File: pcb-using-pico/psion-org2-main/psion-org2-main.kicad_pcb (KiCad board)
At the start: 2 copper layers, 70 x 106 mm, 92 parts, among them J1 Conn_01x24_Female, J2 Conn_01x03_Female, J3 Conn_01x27_Female, SW1 AC_ON, SW10 n, SW11 t, SW12 del, SW13 up, SW14 c, SW15 i, SW16 o, SW17 u, SW18 y, SW19 down, SW2 A, SW20 d, SW21 j, SW22 p, SW23 v, SW24 z, SW25 left, SW26 e, SW27 k, SW28 q, SW29 w, SW3 g, SW30 spc, SW31 right, SW32 f, SW33 L, SW34 r, SW35 x, SW36 exe, SW4 m, SW5 s, SW6 shft, SW7 mode, SW8 b, SW9 h, U1 Pico, U10 AMS1117-3.3, U11 AMS1117-3.3, U2 74HC595, U3 Regulator_Switching_MT3608, U4 74LS165, U5 MCP7940N-xSN, U6 74LS245, U7 74LS245, Y1 32k768Hz

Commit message: Updates to both PCBs
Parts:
- removed C14: C, Capacitor_SMD:C_0805_2012Metric
- removed R14: 4k7, Resistor_SMD:R_0805_2012Metric
- removed R15: R_Small, Resistor_SMD:R_0805_2012Metric
- removed U6, U7: 74LS245, Package_SO:TSSOP-20_4.4x6.5mm_P0.65mm
- removed Y1: 32k768Hz, Crystal:Crystal_SMD_3215-2Pin_3.2x1.5mm
- added D1: SS36, Diode_SMD:D_SOD-123, B.Cu at (77.2, 93.2)
- added TR2: Si2302CDS-n-channel, Package_TO_SOT_SMD:SOT-23, F.Cu at (109.5, 80.3)
- added U8: ESP32-WROOM-32, RF_Module:ESP32-WROOM-32, B.Cu at (123.7, 88.0)
- C1, C10, C11, C12, C17, C18, C19, C2, C20, C21, C22, C3, C4, C5, C6, C7, C8, C9, J2, JP1, L1, R1, R10, R11, R12, R2, R22, R23, R3, R4, TR1, U10, U11, U3: moved to B.Cu
- C13: value C -> 1uF; moved to B.Cu
- R13: value 4k7 -> 10k; moved to B.Cu
- U5: value MCP7940N-xSN -> 74HC595; footprint Package_SO:SO-8_3.9x4.9mm_P1.27mm -> Package_SO:SOIC-16_3.9x9.9mm_P1.27mm; moved to B.Cu
- moved U11 141.8 mm to (125.8, 148.5)
- moved U10 141.7 mm to (125.7, 138.5)
- moved C13 113.4 mm to (75.2, 85.7)
- moved C21 98.1 mm to (84.7, 95.1), turned to 180 degrees
- moved R13 92.8 mm to (71.4, 85.7)
- moved R11 87.8 mm to (77.9, 97.5), turned to 180 degrees
- moved J2 87.2 mm to (75.5, 107.0)
- moved C10 85.6 mm to (80.4, 93.2), turned to 270 degrees
- moved JP1 82.1 mm to (85.3, 91.5)
- moved L1 76.6 mm to (72.6, 90.4)
- moved U5 75.8 mm to (86.0, 140.4)
- moved TR1 75.3 mm to (89.5, 96.6)
- moved R22 71.1 mm to (25.9, 100.2)
- moved U3 71.1 mm to (73.4, 96.0), turned to 180 degrees
- moved C8 69.7 mm to (11.2, 100.9)
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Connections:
- net LATCHOUT renamed LATCHOUT1
- C13 pad 2: GND -> Net-(C13-Pad2)
- J3 pad 10: SPGM -> (no net)
- J3 pad 11: SS -> (no net)
- J3 pad 12: SCLK -> (no net)
- J3 pad 13: SOE -> (no net)
- J3 pad 14: SMR -> (no net)
- J3 pad 15: (no net) -> LS_DIR
- J3 pad 2: SD0 -> (no net)
- J3 pad 3: SD1 -> (no net)
- J3 pad 4: SD2 -> (no net)
- J3 pad 5: SD3 -> (no net)
- J3 pad 6: SD4 -> (no net)
- J3 pad 7: SD5 -> (no net)
- J3 pad 8: SD6 -> (no net)
- J3 pad 9: SD7 -> (no net)
- R13 pad 2: RTC_SDA -> Net-(C13-Pad1)
- U1 pad 1: P_SD0 -> (no net)
- U1 pad 10: P_SD7 -> (no net)
- U1 pad 11: P_SPGM -> PICO_TX
- U1 pad 12: P_SS -> PICO_RX
- U1 pad 14: P_SCLK -> (no net)
- U1 pad 15: P_SOE -> (no net)
- U1 pad 16: P_SMR -> (no net)
- U1 pad 2: P_SD1 -> (no net)
- U1 pad 20: (no net) -> LATCHOUT2
- U1 pad 24: (no net) -> LS_DIR
- U1 pad 34: DRV_HV -> Net-(R22-Pad2)
- U1 pad 4: P_SD2 -> (no net)
- U1 pad 5: P_SD3 -> (no net)
- U1 pad 6: P_SD4 -> (no net)
- U1 pad 7: P_SD5 -> (no net)
- U1 pad 9: P_SD6 -> (no net)
- U5 pad 1: Net-(C14-Pad1) -> ESP_ON
- U5 pad 2: Net-(C13-Pad1) -> (no net)
- U5 pad 3: Net-(R22-Pad2) -> (no net)
- U5 pad 4: GND -> (no net)
- U5 pad 5: RTC_SDA -> (no net)
- U5 pad 6: RTC_SCL -> (no net)
- U5 pad 8: +3V3 -> GND

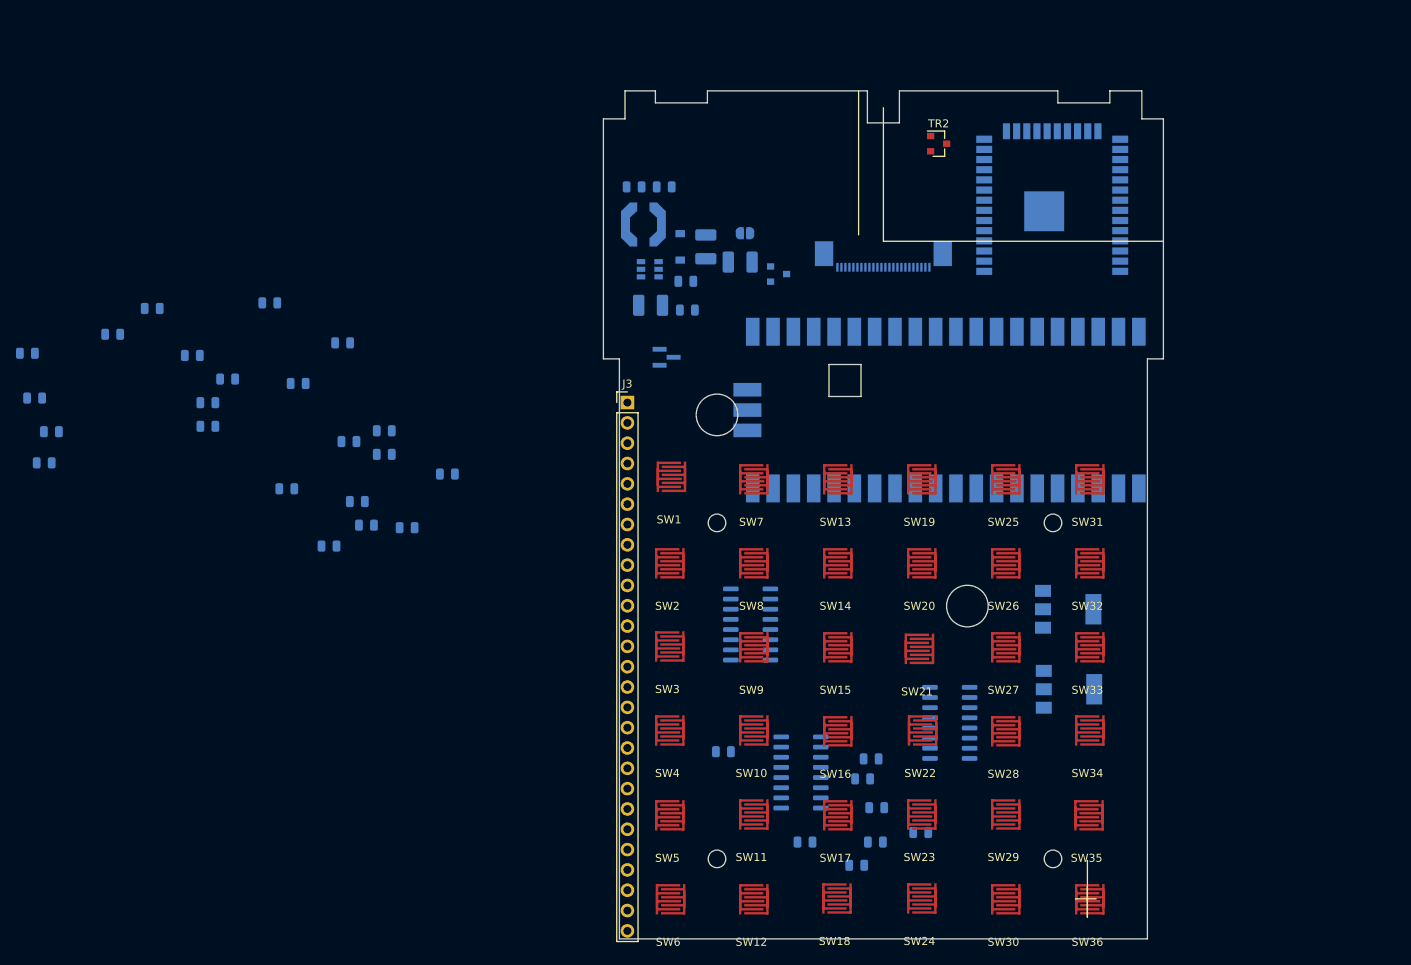
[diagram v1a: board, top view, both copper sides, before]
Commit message: Added second connector, eeprom on power pcb
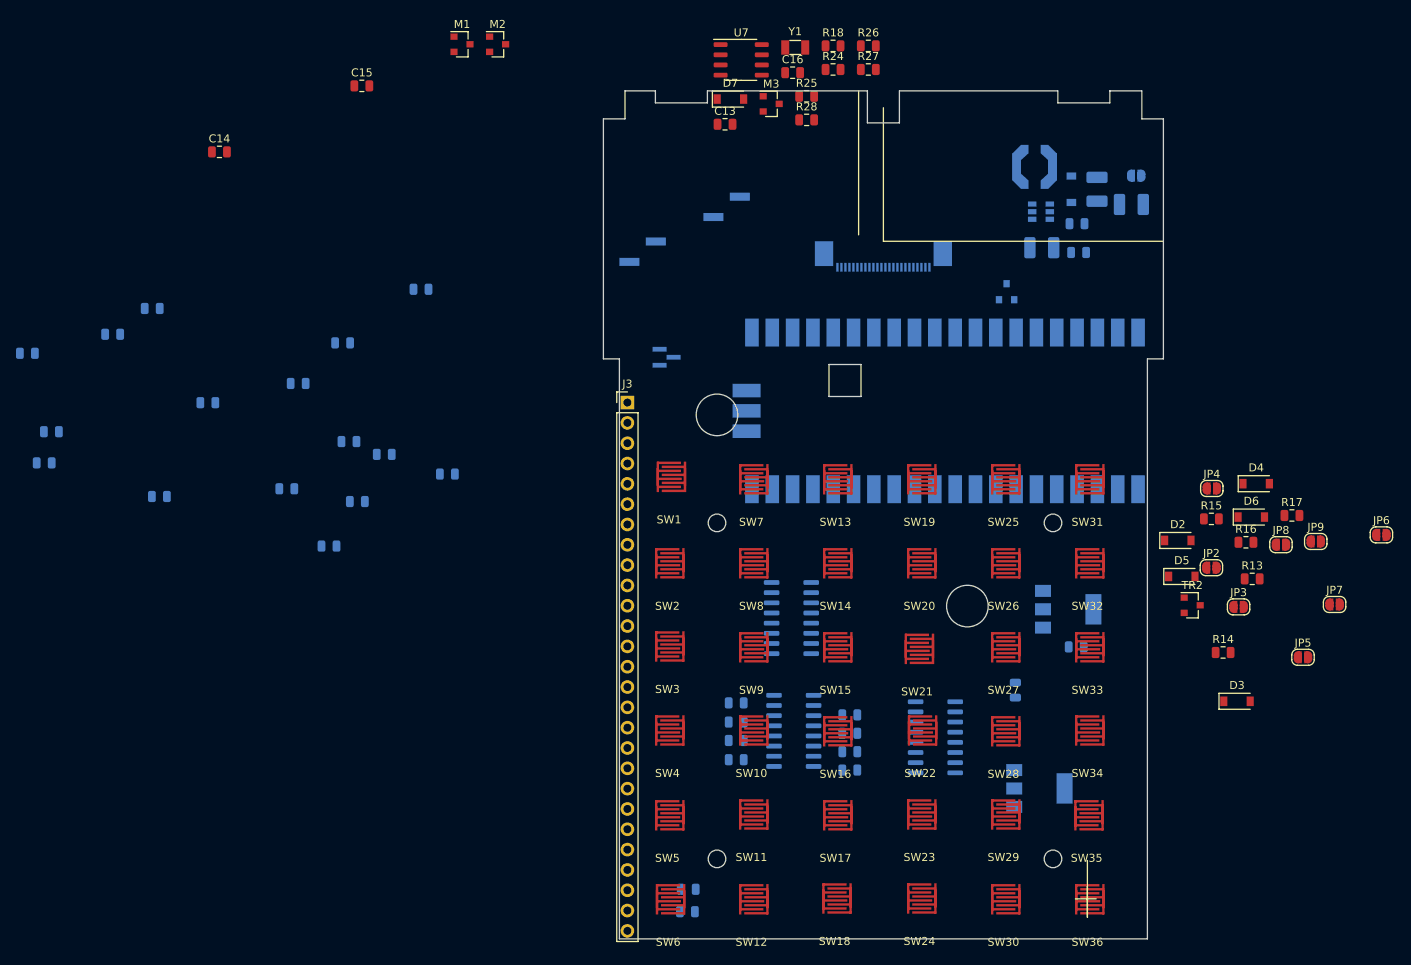
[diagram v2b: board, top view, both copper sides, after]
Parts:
- removed C18, C20: C_Small, Capacitor_SMD:C_0805_2012Metric
- removed U11: AMS1117-3.3, Package_TO_SOT_SMD:SOT-223-3_TabPin2
- removed U8: ESP32-WROOM-32, RF_Module:ESP32-WROOM-32
- added C14: 100n, Capacitor_SMD:C_0805_2012Metric, F.Cu at (19.6, 81.3)
- added C15: 100n, Capacitor_SMD:C_0805_2012Metric, F.Cu at (37.4, 73.1)
- added C16: C, Capacitor_SMD:C_0805_2012Metric, F.Cu at (91.3, 71.4)
- added D2: D_Schottky, Diode_SMD:D_SOD-123, F.Cu at (139.4, 129.9)
- added D3: D, Diode_SMD:D_SOD-123, F.Cu at (146.8, 150.0)
- added D4: D, Diode_SMD:D_SOD-123, F.Cu at (149.2, 122.8)
- added D5: D, Diode_SMD:D_SOD-123, F.Cu at (139.9, 134.4)
- added D6: 4v7, Diode_SMD:D_SOD-123, F.Cu at (148.6, 127.0)
- added D7: 4v7, Diode_SMD:D_SOD-123, F.Cu at (83.5, 74.7)
- added J4: Conn_01x02_Female, Connector_PinHeader_2.54mm:PinHeader_1x02_P2.54mm_Vertical_SMD_Pin1Left, B.Cu at (83.0, 88.2)
- added J5: Conn_01x02_Female, Connector_PinHeader_2.54mm:PinHeader_1x02_P2.54mm_Vertical_SMD_Pin1Left, B.Cu at (72.5, 93.8)
- added JP2: Jumper_NO_Small, Jumper:SolderJumper-2_P1.3mm_Open_RoundedPad1.0x1.5mm, F.Cu at (143.6, 133.3)
- added JP3: Jumper_NO_Small, Jumper:SolderJumper-2_P1.3mm_Open_RoundedPad1.0x1.5mm, F.Cu at (147.0, 138.2)
- added JP4: Jumper_NO_Small, Jumper:SolderJumper-2_P1.3mm_Open_RoundedPad1.0x1.5mm, F.Cu at (143.7, 123.4)
- added JP5: Jumper_NO_Small, Jumper:SolderJumper-2_P1.3mm_Open_RoundedPad1.0x1.5mm, F.Cu at (155.1, 144.5)
- added JP6: Jumper_NO_Small, Jumper:SolderJumper-2_P1.3mm_Open_RoundedPad1.0x1.5mm, F.Cu at (164.8, 129.2)
- added JP7: Jumper_NO_Small, Jumper:SolderJumper-2_P1.3mm_Open_RoundedPad1.0x1.5mm, F.Cu at (159.0, 137.9)
- added JP8: Jumper_NO_Small, Jumper:SolderJumper-2_P1.3mm_Open_RoundedPad1.0x1.5mm, F.Cu at (152.3, 130.4)
- added JP9: Jumper_NO_Small, Jumper:SolderJumper-2_P1.3mm_Open_RoundedPad1.0x1.5mm, F.Cu at (156.6, 130.0)
- added M1: P-CHANNEL-MOSFET, Package_TO_SOT_SMD:SOT-23, F.Cu at (49.9, 67.9)
- added M2: P-CHANNEL-MOSFET, Package_TO_SOT_SMD:SOT-23, F.Cu at (54.4, 67.9)
- added M3: P-CHANNEL-MOSFET, Package_TO_SOT_SMD:SOT-23, F.Cu at (88.6, 75.3)
- added R14: R_Small, Resistor_SMD:R_0805_2012Metric, F.Cu at (145.1, 143.9)
- added R15: R_Small, Resistor_SMD:R_0805_2012Metric, F.Cu at (143.6, 127.2)
- added R16: R_Small, Resistor_SMD:R_0805_2012Metric, F.Cu at (147.9, 130.1)
- added R17: R_Small, Resistor_SMD:R_0805_2012Metric, F.Cu at (153.7, 126.8)
- added R18: R_Small, Resistor_SMD:R_0805_2012Metric, F.Cu at (96.3, 68.1)
- added R24: R_Small, Resistor_SMD:R_0805_2012Metric, F.Cu at (96.3, 71.0)
- added R25: 4k7, Resistor_SMD:R_0805_2012Metric, F.Cu at (93.0, 74.4)
- added R26: 4k7, Resistor_SMD:R_0805_2012Metric, F.Cu at (100.7, 68.1)
- added R27: R_Small, Resistor_SMD:R_0805_2012Metric, F.Cu at (100.7, 71.0)
- added R28: R_Small, Resistor_SMD:R_0805_2012Metric, F.Cu at (93.0, 77.3)
- added U6: AMS1117-5.0, Package_TO_SOT_SMD:SOT-223-3_TabPin2, B.Cu at (122.1, 160.9)
- added U7: MCP7940N-xSN, Package_SO:SO-8_3.9x4.9mm_P1.27mm, F.Cu at (84.8, 69.8)
- added Y1: 32k768Hz, Crystal:Crystal_SMD_3215-2Pin_3.2x1.5mm, F.Cu at (91.6, 68.3)
- C13: value 1uF -> C; moved to F.Cu
- C17, C19: value C_Small -> 100n
- R13: value 10k -> R_Small; moved to F.Cu
- moved C17 127.9 mm to (119.1, 148.6), turned to 270 degrees
- moved R22 92.3 mm to (78.1, 176.3)
- moved R13 91.5 mm to (148.7, 134.7)
- moved C19 90.0 mm to (126.7, 143.2), turned to 180 degrees
- moved TR2 65.8 mm to (141.2, 138.0)
- moved R23 57.3 mm to (78.2, 173.5), turned to 180 degrees
- moved C10 49.4 mm to (129.3, 86.0)
- moved C4 49.4 mm to (122.4, 93.3)
- moved L1 49.4 mm to (121.5, 83.2)
- moved R12 49.4 mm to (127.0, 93.9)
- moved C21 49.4 mm to (133.6, 87.9)
- moved D1 49.4 mm to (126.1, 86.0)
- moved JP1 49.4 mm to (134.2, 84.3)
- moved R11 49.4 mm to (126.8, 90.3)
- moved U3 49.4 mm to (122.3, 88.8)
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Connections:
- C13 pad 2: Net-(C13-Pad2) -> GND
- C17 pad 1: VBAT -> VBAT_SWITCHED1
- C19 pad 1: VccPico -> +3V3
- C4 pad 1: +3V3 -> Net-(C4-Pad1)
- J3 pad 17: (no net) -> ESP_ON
- J3 pad 18: (no net) -> PICO_TX
- J3 pad 19: (no net) -> PICO_RX
- J3 pad 20: (no net) -> OLED_SCL
- J3 pad 21: (no net) -> OLED_SDA
- J3 pad 22: (no net) -> EX_ON
- J3 pad 23: (no net) -> VBAT_SWITCHED2
- J3 pad 24: (no net) -> 5V_ON
- J3 pad 25: (no net) -> 5V
- L1 pad 1: +3V3 -> Net-(C4-Pad1)
- R13 pad 1: +3V3 -> Net-(D3-Pad1)
- R13 pad 2: Net-(C13-Pad1) -> GND
- SW1 pad 1: +3V3 -> Net-(JP8-Pad2)
- TR2 pad 1: ESP_ON -> Net-(D3-Pad1)
- TR2 pad 3: Net-(C13-Pad2) -> Net-(M2-Pad1)
- U1 pad 19: (no net) -> SDAOUT
- U1 pad 32: SDAOUT -> VBAT_SW_ON
- U1 pad 39: (no net) -> Net-(D2-Pad1)
- U10 pad 2: VccPico -> +3V3
- U10 pad 3: VBAT -> VBAT_SWITCHED1
- U3 pad 4: +3V3 -> Net-(C4-Pad1)
- U3 pad 5: +3V3 -> Net-(C4-Pad1)
- U5 pad 2: (no net) -> BUZZER
- U5 pad 3: (no net) -> 5V_ON

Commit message: Start of PCB layout
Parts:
- added D8: D, Diode_SMD:D_SOD-123, F.Cu at (198.3, 39.1)
- added D9: D, Diode_SMD:D_SOD-123, F.Cu at (202.1, 43.8)
- added J6: Conn_01x11_Female, Connector_PinHeader_2.54mm:PinHeader_1x11_P2.54mm_Vertical, F.Cu at (140.2, 61.0)
- added JP10: Jumper_NO_Small, Jumper:SolderJumper-2_P1.3mm_Open_RoundedPad1.0x1.5mm, F.Cu at (193.7, 38.0)
- C14: moved to B.Cu
- moved C14 150.3 mm to (162.0, 129.4)
- moved M2 137.2 mm to (187.2, 33.5)
- moved M1 134.4 mm to (180.5, 36.1)
- moved M3 103.0 mm to (185.2, 39.6)
- moved D5 94.3 mm to (226.8, 97.9)
- moved R28 92.4 mm to (181.3, 50.2)
- moved R18 90.9 mm to (183.9, 43.9)
- moved R24 87.4 mm to (178.2, 40.5)
- moved J5 86.1 mm to (157.0, 77.2)
- moved D6 85.4 mm to (229.9, 101.0)
- moved JP9 85.2 mm to (239.8, 111.6)
- moved R27 79.1 mm to (176.0, 46.8)
- moved D4 78.3 mm to (224.4, 100.9)
- moved J3 73.2 mm to (141.5, 94.3)
- moved C17 73.0 mm to (189.8, 130.6)
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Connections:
- J3 pad 15: LS_DIR -> (no net)
- J3 pad 17: ESP_ON -> LS_DIR
- J3 pad 18: PICO_TX -> SD_OE
- J3 pad 19: PICO_RX -> SC_OE
- J3 pad 20: OLED_SCL -> EXT_PWR_IN
- J3 pad 21: OLED_SDA -> ESP_ON
- M2 pad 2: VBAT -> Net-(D8-Pad1)
- M3 pad 2: VBAT -> Net-(D8-Pad1)
- R14 pad 1: VBAT -> Net-(D8-Pad1)
- R18 pad 1: VBAT -> Net-(D8-Pad1)
- R24 pad 1: VBAT -> Net-(D8-Pad1)
- U1 pad 38: (no net) -> GND
- U5 pad 6: (no net) -> SD_OE
- U5 pad 7: (no net) -> SC_OE
